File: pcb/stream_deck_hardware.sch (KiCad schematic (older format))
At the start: 1 part

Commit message: Schematic upgrade
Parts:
- added C? (x3): 4.7uF, symbol Device:C
- added C? (x6): 100nF, symbol Device:C
- added C?: 0,1uF, symbol Device:C
- added C?: 2,2uF, symbol Device:CP
- added P?: USB_C_Plug, symbol Connector:USB_C_Plug
- added U?: LF33_TO252, Package_TO_SOT_SMD:TO-252-2, symbol Regulator_Linear:LF33_TO252
- added Y?: Crystal_Small, symbol Device:Crystal_Small
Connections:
- net labels added: +3.3V, Button_1, Button_2, Button_3, Button_4, Button_5, Button_6, Button_7, Button_8, Button_9, ENC_01_A, ENC_01_B, ENC_01_btn, ENC_02_A, ENC_02_B, ENC_02_btn, ENC_03_A, ENC_03_B, ENC_03_btn, GND, JACK_button, RST, VBUS
- wire segments 0 -> 44
- no-connect marks 1 -> 10
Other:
- moved on the sheet: U?

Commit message: Added boot pins jumper selector
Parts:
- added J?: Conn_BOOT, Connector_PinHeader_2.54mm:PinHeader_2x03_P2.54mm_Vertical, symbol Connector_Generic:Conn_02x03_Counter_Clockwise
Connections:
- net labels added: BOOT0, BOOT1
- wire segments 44 -> 56
- no-connect marks 10 -> 9
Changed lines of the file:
@@
 NoConn ~ 3250 4700
 NoConn ~ 3250 4800
-NoConn ~ 4650 1900
 Wire Wire Line
 	6750 2050 6850 2050
@@
 Wire Wire Line
 	3250 2800 3400 2800
+Text GLabel 6050 2450 0    50   Input ~ 0
+BOOT0
+Wire Wire Line
+	6050 2450 6250 2450
+Text GLabel 7750 4150 2    50   Input ~ 0
+BOOT1
+Wire Wire Line
+	7750 4150 7550 4150
+Text GLabel 3820 1620 0    50   Input ~ 0
+BOOT0
+$Comp
+L Connector_Generic:Conn_02x03_Counter_Clockwise J?
+U 1 1 6197877E
+P 4120 1620
+F 0 "J?" H 4170 1937 50  0000 C CNN
+F 1 "Conn_BOOT" H 4170 1846 50  0000 C CNN
+F 2 "Connector_PinHeader_2.54mm:PinHeader_2x03_P2.54mm_Vertical" H 4120 1620 50  0001 C CNN
+F 3 "~" H 4120 1620 50  0001 C CNN
+	1    4120 1620
+	1    0    0    -1
+$EndComp
+$Comp
+L power:GND #PWR?
+U 1 1 61986215
+P 4520 1830
+F 0 "#PWR?" H 4520 1580 50  0001 C CNN
+F 1 "GND" H 4525 1657 50  0000 C CNN
+F 2 "" H 4520 1830 50  0001 C CNN
+F 3 "" H 4520 1830 50  0001 C CNN
+	1    4520 1830
+	1    0    0    -1
+$EndComp
+Wire Wire Line
+	4420 1720 4520 1720
+Wire Wire Line
+	4520 1720 4520 1830
+$Comp
+L power:GND #PWR?
+U 1 1 6198ABFD
+P 3820 1830
+F 0 "#PWR?" H 3820 1580 50  0001 C CNN
+F 1 "GND" H 3825 1657 50  0000 C CNN
+F 2 "" H 3820 1830 50  0001 C CNN
+F 3 "" H 3820 1830 50  0001 C CNN
+	1    3820 1830
+	-1   0    0    -1
+$EndComp
+Wire Wire Line
+	3920 1720 3820 1720
+Wire Wire Line
+	3820 1720 3820 1830
+Wire Wire Line
+	4520 1520 4520 1410
+Wire Wire Line
+	4420 1520 4520 1520
+$Comp
+L power:+3.3V #PWR?
+U 1 1 61995457
+P 4520 1410
+F 0 "#PWR?" H 4520 1160 50  0001 C CNN
+F 1 "+3.3V" H 4535 1583 50  0000 C CNN
+F 2 "" H 4520 1410 50  0001 C CNN
+F 3 "" H 4520 1410 50  0001 C CNN
+	1    4520 1410
+	-1   0    0    -1
+$EndComp
+Wire Wire Line
+	3920 1520 3820 1520
+Wire Wire Line
+	3820 1520 3820 1410
+$Comp
+L power:+3.3V #PWR?
+U 1 1 6199E8B3
+P 3820 1410
+F 0 "#PWR?" H 3820 1160 50  0001 C CNN
+F 1 "+3.3V" H 3835 1583 50  0000 C CNN
+F 2 "" H 3820 1410 50  0001 C CNN
+F 3 "" H 3820 1410 50  0001 C CNN
+	1    3820 1410
+	-1   0    0    -1
+$EndComp
+Text GLabel 4520 1620 2    50   Input ~ 0
+BOOT1
+Wire Wire Line
+	3820 1620 3920 1620
+Wire Wire Line
+	4420 1620 4520 1620
 $EndSCHEMATC

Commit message: Schematic update
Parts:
- removed P?: USB_C_Plug, symbol Connector:USB_C_Plug
- added J?: USB_C_Receptacle_USB2.0, Connector_USB:USB_C_Receptacle_Palconn_UTC16-G, symbol Connector:USB_C_Receptacle_USB2.0
- added R? (x4): R, symbol Device:R
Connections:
- net labels added: USB_DM, USB_DP
- wire segments 56 -> 81
- no-connect marks 9 -> 3
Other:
- moved on the sheet: C?

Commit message: Schematic version 1.0
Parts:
- added C?: 0.1uF, symbol Device:C
- added J? (x2): Conn_01x04_Male, symbol Connector:Conn_01x04_Male
- added JP? (x3): SolderJumper_2_Bridged, symbol Jumper:SolderJumper_2_Bridged
- added R?: R, symbol Device:R
- added U?: 74LVC1G332, symbol 74xGxx:74LVC1G332
- R? (x2): value R -> 5.1k
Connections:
- net +3V3: now also R?.2
- net Button_1: now also U?.8 (PC0), U?.6
- net Button_2: now also U?.9 (PC1)
- net Button_3: now also U?.10 (PC2)
- net Button_4: now also U?.11 (PC3)
- net Button_5: now also U?.24 (PC4), U?.1
- net Button_6: now also U?.25 (PC5)
- net Button_7: now also U?.37 (PC6)
- net Button_8: now also U?.38 (PC7)
- net Button_9: now also U?.39 (PC8), U?.3
- net ENC_01_A: now also U?.14 (PA0)
- net ENC_01_B: now also U?.15 (PA1)
- net ENC_01_btn: now also U?.51 (PC10)
- net ENC_02_A: now also U?.22 (PA6)
- net ENC_02_B: now also U?.23 (PA7)
- net ENC_02_btn: now also U?.52 (PC11)
- net ENC_03_A: now also U?.41 (PA8)
- net ENC_03_B: now also U?.42 (PA9)
- net ENC_03_btn: now also U?.53 (PC12)
- net GND: now also C?.2, J?.4 (Pin_4), J?.4 (Pin_4), U?.2 (GND)
- net JACK_button: now also U?.40 (PC9)
- net RST: now also C?.1, JP?.2 (B), R?.1
- net USB_DM: now also J?.2 (Pin_2), JP?.2 (B); no longer J?.A7 (D-), J?.B7 (D-)
- net USB_DP: now also J?.3 (Pin_3), JP?.2 (B); no longer J?.A6 (D+), J?.B6 (D+)
- net SWD_DIO: now reaches U?.46 (PA13)
- net SWD_DIO: now also J?.2 (Pin_2)
- net SWD_CLK: now reaches U?.49 (PA14)
- net SWD_CLK: now also J?.3 (Pin_3)
- net EXTERNAL_LEDS: now reaches U?.61 (PB8)
- net AMBILIGHT_LEDS: now reaches U?.62 (PB9)
- net VBUS renamed +5V
- net +5V: now also J?.1 (Pin_1), J?.1 (Pin_1)
- new net: J?.A6 (D+), J?.B6 (D+), JP?.1 (A)
- new net: J?.A7 (D-), J?.B7 (D-), JP?.1 (A)
- new net: JP?.1 (A), U?.4
- new net VCC: U?.5 (VCC)
- no-connect marks 3 -> 2
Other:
- note added: "HARDWARE RESET\n"
- moved on the sheet: C?, J?, R?, U?

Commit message: Added EEPROM memory & some footprints
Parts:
- added R6, R7, R8: 4k7, symbol Device:R
- added U4, U5: AT24CS02-STUM, Package_TO_SOT_SMD:SOT-23-5, symbol Memory_EEPROM:AT24CS02-STUM
- J3, J4: renamed from J?; footprint (none) -> Connector_PinHeader_2.54mm:PinHeader_1x04_P2.54mm_Vertical
- JP1, JP2, JP3: renamed from JP?; footprint (none) -> Jumper:SolderJumper-2_P1.3mm_Bridged2Bar_RoundedPad1.0x1.5mm
- U3: renamed from U?; footprint (none) -> Package_TO_SOT_SMD:SOT-23-6
- gave numbers to parts that had none: 22
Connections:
- net +3V3: now also R6.1, R7.1, R8.1, U4.4 (VCC), U5.4 (VCC)
- net GND: now also U4.2 (GND), U5.2 (GND)
- new net I2C_SCL_EEPROM: R7.2, U4.1 (SCL), U5.1 (SCL)
- new net I2C_SCL_WP: R8.2, U4.5 (WP), U5.5 (WP)
- new net I2C_SDA_EEPROM: R6.2, U4.3 (SDA), U5.3 (SDA)
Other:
- moved on the sheet: J3, J4

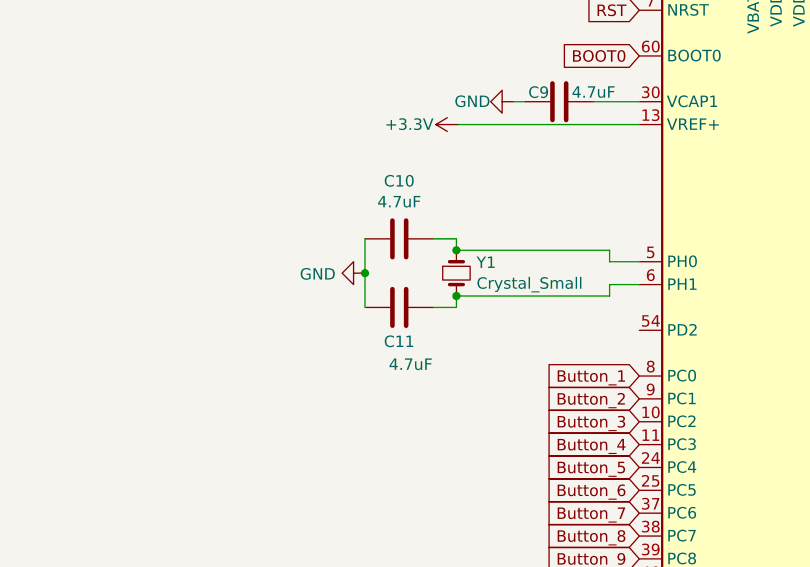
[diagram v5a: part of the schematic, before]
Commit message: Finish schematic and added footprints
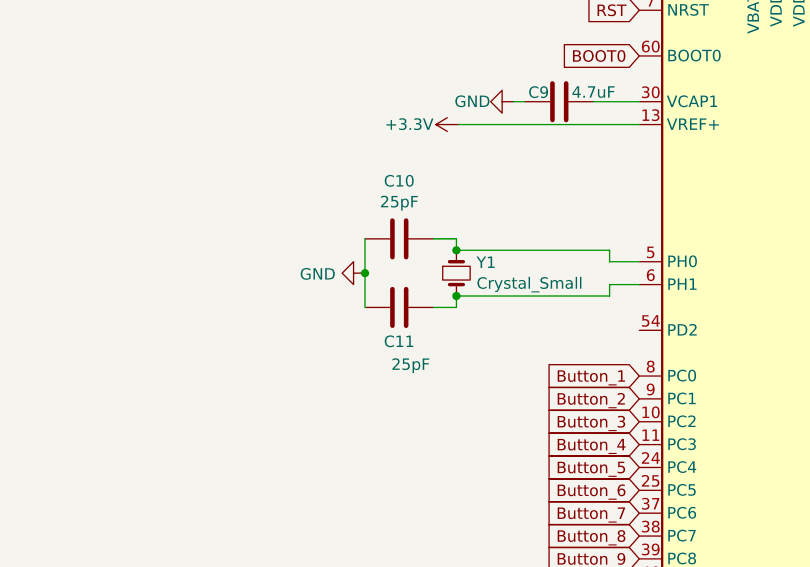
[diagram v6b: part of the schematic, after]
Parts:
- C1, C12, C2, C3, C4, C5, C6, C7, C8, C9: footprint (none) -> Capacitor_SMD:C_0603_1608Metric
- C10, C11: value 4.7uF -> 25pF; footprint (none) -> Capacitor_SMD:C_0603_1608Metric
- R1, R2, R3, R4, R5, R6, R7, R8: footprint (none) -> Resistor_SMD:R_0603_1608Metric
- Y1: footprint (none) -> Crystal:Crystal_HC49-U_Vertical
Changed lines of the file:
@@
 F 0 "C1" H 6065 1046 50  0000 L CNN
 F 1 "100nF" H 6065 955 50  0000 L CNN
-F 2 "" H 5988 850 50  0001 C CNN
+F 2 "Capacitor_SMD:C_0603_1608Metric" H 5988 850 50  0001 C CNN
 F 3 "~" H 5950 1000 50  0001 C CNN
 	1    5950 1000
@@
 F 0 "C2" H 6465 1046 50  0000 L CNN
 F 1 "100nF" H 6465 955 50  0000 L CNN
-F 2 "" H 6388 850 50  0001 C CNN
+F 2 "Capacitor_SMD:C_0603_1608Metric" H 6388 850 50  0001 C CNN
 F 3 "~" H 6350 1000 50  0001 C CNN
 	1    6350 1000
@@
 F 0 "C3" H 6865 1046 50  0000 L CNN
 F 1 "100nF" H 6865 955 50  0000 L CNN
-F 2 "" H 6788 850 50  0001 C CNN
+F 2 "Capacitor_SMD:C_0603_1608Metric" H 6788 850 50  0001 C CNN
 F 3 "~" H 6750 1000 50  0001 C CNN
 	1    6750 1000
@@
 F 0 "C4" H 7265 1046 50  0000 L CNN
 F 1 "100nF" H 7265 955 50  0000 L CNN
-F 2 "" H 7188 850 50  0001 C CNN
+F 2 "Capacitor_SMD:C_0603_1608Metric" H 7188 850 50  0001 C CNN
 F 3 "~" H 7150 1000 50  0001 C CNN
 	1    7150 1000
@@
 F 0 "C5" H 7665 1046 50  0000 L CNN
 F 1 "100nF" H 7665 955 50  0000 L CNN
-F 2 "" H 7588 850 50  0001 C CNN
+F 2 "Capacitor_SMD:C_0603_1608Metric" H 7588 850 50  0001 C CNN
 F 3 "~" H 7550 1000 50  0001 C CNN
 	1    7550 1000
@@
 F 0 "C6" H 8065 1046 50  0000 L CNN
 F 1 "100nF" H 8065 955 50  0000 L CNN
-F 2 "" H 7988 850 50  0001 C CNN
+F 2 "Capacitor_SMD:C_0603_1608Metric" H 7988 850 50  0001 C CNN
 F 3 "~" H 7950 1000 50  0001 C CNN
 	1    7950 1000
@@
 F 0 "C7" H 9315 1086 50  0000 L CNN
 F 1 "0,1uF" H 9315 995 50  0000 L CNN
-F 2 "" H 9238 890 50  0001 C CNN
+F 2 "Capacitor_SMD:C_0603_1608Metric" H 9238 890 50  0001 C CNN
 F 3 "~" H 9200 1040 50  0001 C CNN
 	1    9200 1040
@@
 F 0 "C8" H 10568 1086 50  0000 L CNN
 F 1 "2,2uF" H 10568 995 50  0000 L CNN
-F 2 "" H 10488 890 50  0001 C CNN
+F 2 "Capacitor_SMD:C_0603_1608Metric" H 10488 890 50  0001 C CNN
 F 3 "~" H 10450 1040 50  0001 C CNN
 	1    10450 1040
@@
 F 0 "Y1" V 5404 3488 50  0000 L CNN
 F 1 "Crystal_Small" V 5495 3488 50  0000 L CNN
-F 2 "" H 5450 3400 50  0001 C CNN
+F 2 "Crystal:Crystal_HC49-U_Vertical" H 5450 3400 50  0001 C CNN
 F 3 "~" H 5450 3400 50  0001 C CNN
 	1    5450 3400
@@
 P 5200 3250
 F 0 "C10" V 4948 3250 50  0000 C CNN
-F 1 "4.7uF" V 5039 3250 50  0000 C CNN
-F 2 "" H 5238 3100 50  0001 C CNN
+F 1 "25pF" V 5039 3250 50  0000 C CNN
+F 2 "Capacitor_SMD:C_0603_1608Metric" H 5238 3100 50  0001 C CNN
 F 3 "~" H 5200 3250 50  0001 C CNN
 	1    5200 3250
@@
 P 5200 3550
 F 0 "C11" V 5350 3550 50  0000 C CNN
-F 1 "4.7uF" V 5450 3600 50  0000 C CNN
-F 2 "" H 5238 3400 50  0001 C CNN
+F 1 "25pF" V 5450 3600 50  0000 C CNN
+F 2 "Capacitor_SMD:C_0603_1608Metric" H 5238 3400 50  0001 C CNN
 F 3 "~" H 5200 3550 50  0001 C CNN
 	1    5200 3550
@@
 F 0 "R2" H 4740 1666 50  0000 L CNN
 F 1 "R" H 4740 1575 50  0000 L CNN
-F 2 "" V 4600 1620 50  0001 C CNN
+F 2 "Resistor_SMD:R_0603_1608Metric" V 4600 1620 50  0001 C CNN
 F 3 "~" H 4670 1620 50  0001 C CNN
 	1    4670 1620
@@
 F 0 "R4" V 2260 3230 50  0000 L CNN
 F 1 "5.1k" V 2260 3370 50  0000 L CNN
-F 2 "" V 2110 3340 50  0001 C CNN
+F 2 "Resistor_SMD:R_0603_1608Metric" V 2110 3340 50  0001 C CNN
 F 3 "~" H 2180 3340 50  0001 C CNN
 	1    2180 3340
@@
 F 0 "R3" V 2250 3250 50  0000 L CNN
 F 1 "5.1k" V 2250 3050 50  0000 L CNN
-F 2 "" V 2110 3240 50  0001 C CNN
+F 2 "Resistor_SMD:R_0603_1608Metric" V 2110 3240 50  0001 C CNN
 F 3 "~" H 2180 3240 50  0001 C CNN
 	1    2180 3240
@@
 F 0 "C9" V 5940 2740 50  0000 C CNN
 F 1 "4.7uF" V 5970 2500 50  0000 C BNN
-F 2 "" H 5938 2500 50  0001 C CNN
+F 2 "Capacitor_SMD:C_0603_1608Metric" H 5938 2500 50  0001 C CNN
 F 3 "~" H 5900 2650 50  0001 C CNN
 	1    5900 2650
@@
 F 0 "R1" H 3740 1690 50  0000 L CNN
 F 1 "R" H 3740 1575 50  0000 L CNN
-F 2 "" V 3600 1620 50  0001 C CNN
+F 2 "Resistor_SMD:R_0603_1608Metric" V 3600 1620 50  0001 C CNN
 F 3 "~" H 3670 1620 50  0001 C CNN
 	1    3670 1620
@@
 F 0 "R5" H 10280 4054 50  0000 R CNN
 F 1 "R" H 10280 4145 50  0000 R CNN
-F 2 "" V 10280 4100 50  0001 C CNN
+F 2 "Resistor_SMD:R_0603_1608Metric" V 10280 4100 50  0001 C CNN
 F 3 "~" H 10350 4100 50  0001 C CNN
 	1    10350 4100
@@
 F 0 "C12" H 10465 4556 50  0000 L CNN
 F 1 "0.1uF" H 10465 4465 50  0000 L CNN
-F 2 "" H 10388 4360 50  0001 C CNN
+F 2 "Capacitor_SMD:C_0603_1608Metric" H 10388 4360 50  0001 C CNN
 F 3 "~" H 10350 4510 50  0001 C CNN
 	1    10350 4510
@@
 F 0 "R6" V 2180 5790 50  0000 L CNN
 F 1 "4k7" V 2180 5930 50  0000 L CNN
-F 2 "" V 2030 5900 50  0001 C CNN
+F 2 "Resistor_SMD:R_0603_1608Metric" V 2030 5900 50  0001 C CNN
 F 3 "~" H 2100 5900 50  0001 C CNN
 	1    2100 5900
@@
 F 0 "R7" V 2480 5790 50  0000 L CNN
 F 1 "4k7" V 2480 5930 50  0000 L CNN
-F 2 "" V 2330 5900 50  0001 C CNN
+F 2 "Resistor_SMD:R_0603_1608Metric" V 2330 5900 50  0001 C CNN
 F 3 "~" H 2400 5900 50  0001 C CNN
 	1    2400 5900
@@
 F 0 "R8" V 2780 5790 50  0000 L CNN
 F 1 "4k7" V 2780 5930 50  0000 L CNN
-F 2 "" V 2630 5900 50  0001 C CNN
+F 2 "Resistor_SMD:R_0603_1608Metric" V 2630 5900 50  0001 C CNN
 F 3 "~" H 2700 5900 50  0001 C CNN
 	1    2700 5900
